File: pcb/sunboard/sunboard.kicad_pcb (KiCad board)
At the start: 2 copper layers, 311 parts, among them SW1 SW_Push, SW10 SW_Push, SW100 SW_Push, SW101 SW_Push, SW102 SW_Push, SW103 SW_Push, SW104 SW_Push, SW105 SW_Push, SW106 SW_Push, SW107 SW_Push, SW108 SW_Push, SW109 SW_Push, SW11 SW_Push, SW110 SW_Push, SW111 SW_Push, SW112 SW_Push, SW113 SW_Push, SW114 SW_Push, SW115 SW_Push, SW116 SW_Push, SW117 SW_Push, SW118 SW_Push, SW119 SW_Push, SW12 SW_Push, SW120 SW_Push, SW121 SW_Push, SW122 SW_Push, SW123 SW_Push, SW124 SW_Push, SW125 SW_Push, SW126 SW_Push, SW127 SW_Push, SW128 SW_Push, SW129 SW_Push, SW13 SW_Push, SW130 SW_Push, SW131 SW_Push, SW132 SW_Push, SW133 SW_Push, SW134 SW_Push, SW135 SW_Push, SW136 SW_Push, SW137 SW_Push, SW138 SW_Push, SW139 SW_Push, SW14 SW_Push, SW140 SW_Push, SW141 SW_Push, SW142 SW_Push, SW143 SW_Push, SW144 SW_Push, SW145 SW_Push, SW146 SW_Push, SW147 SW_Push, SW148 SW_Push, SW149 SW_Push, SW15 SW_Push, SW150 SW_Push, SW151 SW_Push, SW152 SW_Push, SW153 SW_Push, SW154 SW_Push, SW16 SW_Push, SW17 SW_Push, SW18 SW_Push, SW19 SW_Push, SW2 SW_Push, SW20 SW_Push, SW21 SW_Push, SW22 SW_Push, SW23 SW_Push, SW24 SW_Push, SW25 SW_Push, SW26 SW_Push, SW27 SW_Push, SW28 SW_Push, SW29 SW_Push, SW3 SW_Push, SW30 SW_Push, SW31 SW_Push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

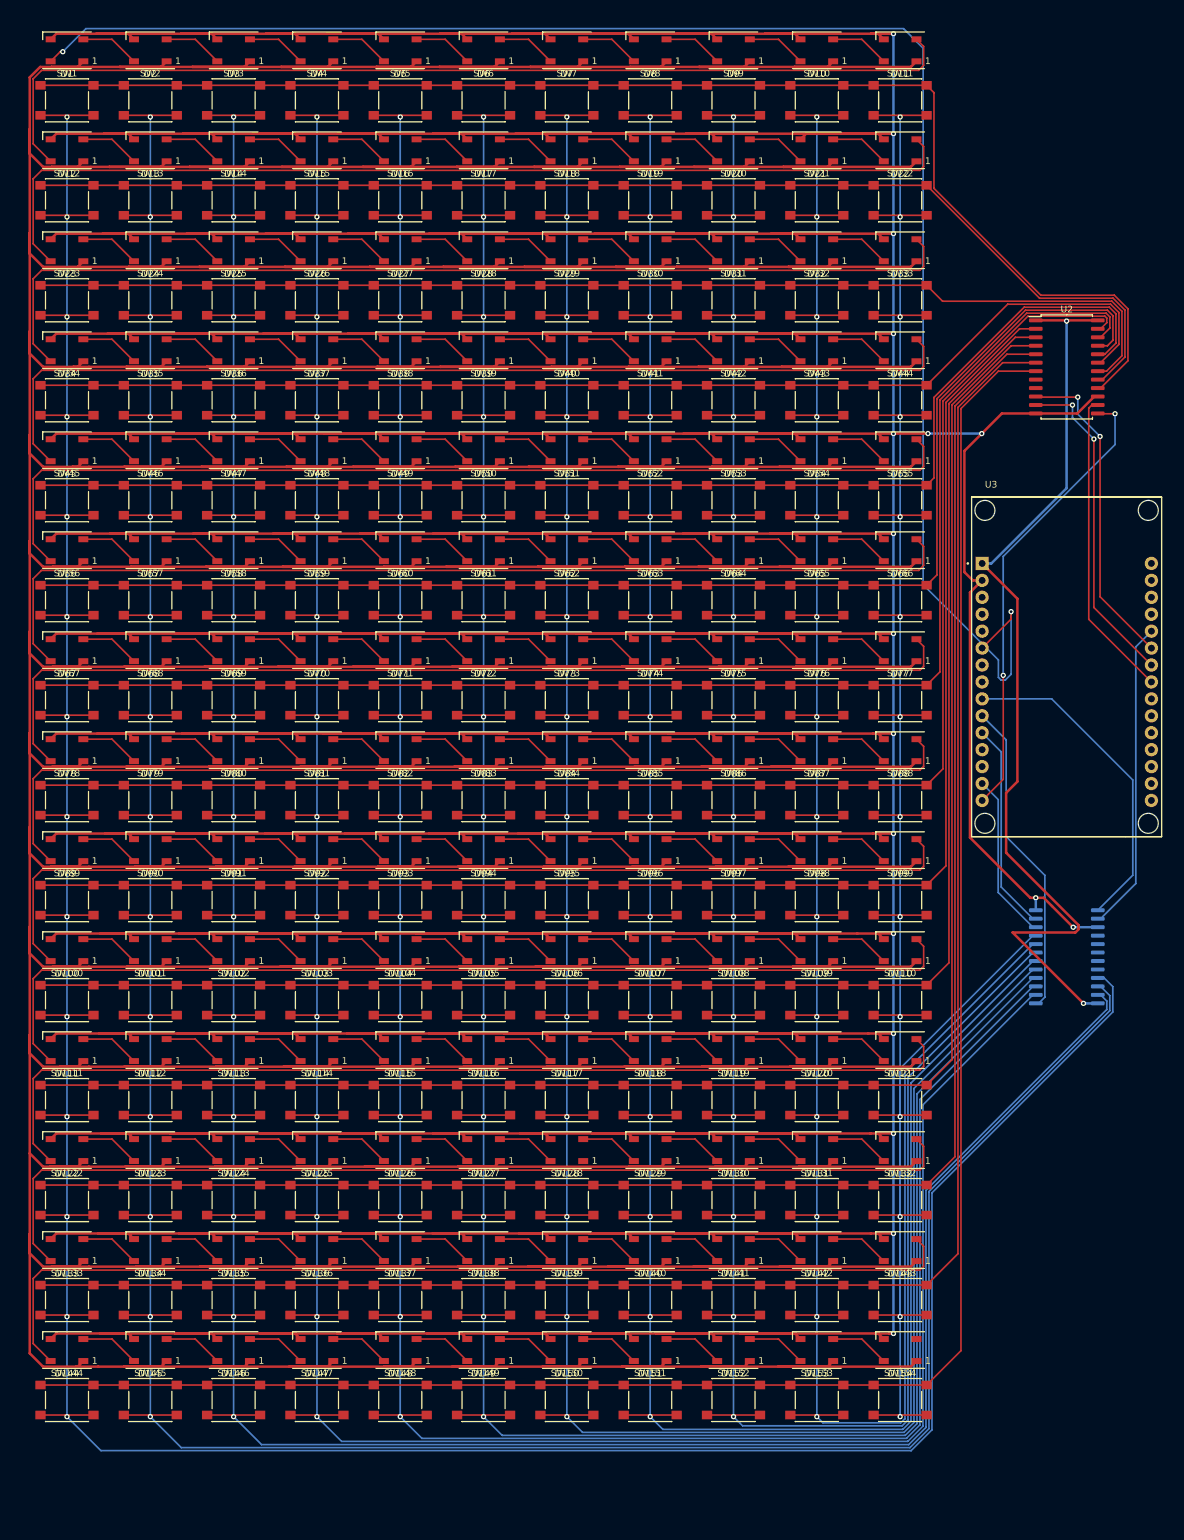
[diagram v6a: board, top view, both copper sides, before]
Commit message: feat(pcb): add display
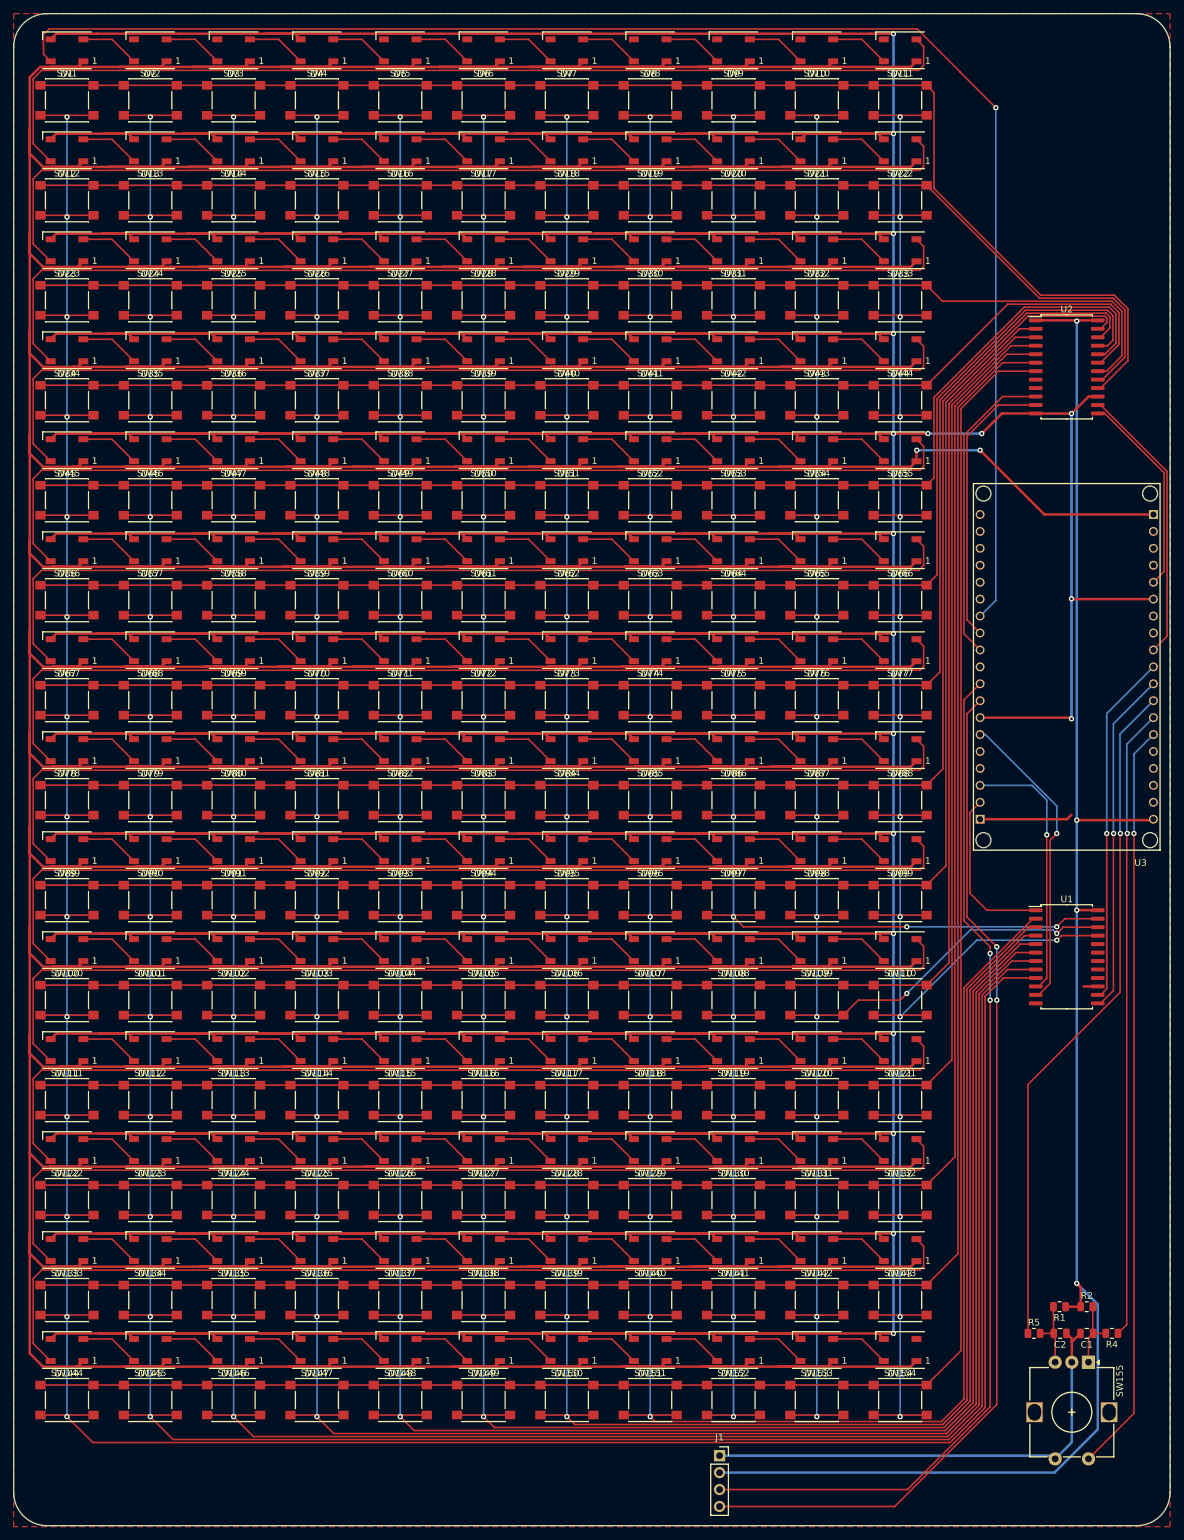
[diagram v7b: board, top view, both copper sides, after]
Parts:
- added C1: 100n, Capacitor_SMD:C_0805_2012Metric, F.Cu at (173.0, 210.0)
- added C2: 100n, Capacitor_SMD:C_0805_2012Metric, F.Cu at (169.0, 210.0)
- added J1: Conn_01x04_Socket, Connector_PinSocket_2.54mm:PinSocket_1x04_P2.54mm_Vertical, F.Cu at (117.9, 228.4)
- added R1: 10k, Resistor_SMD:R_0805_2012Metric, F.Cu at (168.9, 206.0)
- added R2: 10k, Resistor_SMD:R_0805_2012Metric, F.Cu at (173.0, 206.0)
- added R4: 10k, Resistor_SMD:R_0805_2012Metric, F.Cu at (176.8, 210.0)
- added R5: 10k, Resistor_SMD:R_0805_2012Metric, F.Cu at (165.1, 210.0)
- added SW155: RotaryEncoder_Switch, Rotary_Encoder:RotaryEncoder_Alps_EC12E-Switch_Vertical_H20mm, F.Cu at (173.3, 214.3)
- U1: moved to F.Cu
- U3: value ESP32-DEVKIT-V1 -> ESP32_NODEMCU; footprint ESP32-DEVKIT-V1:MODULE_ESP32_DEVKIT_V1 -> ESP32_NODEMCU:MODULE_ESP32_NODEMCU
- turned U3 to 180 degrees
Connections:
- U1 pad 2: Col4 -> Col8
- U1 pad 21: Col1 -> Col11
- U1 pad 22: Col2 -> Col10
- U1 pad 23: Col3 -> Col9
- U1 pad 3: Col5 -> Col7
- U1 pad 5: Col7 -> Col5
- U1 pad 6: Col8 -> Col4
- U1 pad 7: Col9 -> Col3
- U1 pad 8: Col10 -> Col2
- U1 pad 9: Col11 -> Col1
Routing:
- net SCL: track 0.00 -> 156.8 mm, vias 0 -> 2
- net SDA: track 0.00 -> 156.2 mm, vias 0 -> 2
- net VCC: track 141.4 -> 256.9 mm, vias 2 -> 4
- net ROT_BTN: track 0.00 -> 112.7 mm, vias 0 -> 1
- net ROT_B: track 0.00 -> 102.8 mm, vias 0 -> 1
- net ROT_A: track 0.00 -> 94.6 mm, vias 0 -> 1
- net Col9: track 414.6 -> 365.0 mm, vias 14 -> 16
- net Col10: track 402.6 -> 353.3 mm, vias 14 -> 16
- net +5V: track 3047.1 -> 3095.3 mm, vias 0 -> 2
- net R_SEL4: track 68.9 -> 30.7 mm, vias 2 -> 0
- net STATE: track 47.9 -> 25.2 mm
- net LED_IN: track 252.3 -> 229.9 mm, vias 2 -> 1
- net GND: track 2979.0 -> 2995.6 mm, vias 18 -> 19
- net C_SEL3: track 25.1 -> 39.4 mm, vias 0 -> 1
- net C_SEL4: track 31.5 -> 45.4 mm, vias 0 -> 1
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- added copper zone on F.Cu, net GND
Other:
- board outline added: 173.5 x 226.9 mm
